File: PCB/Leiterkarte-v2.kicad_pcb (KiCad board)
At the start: 4 copper layers, 82 parts, among them J1 MSD-1-A, SW33V1 Conn_01x01_Pin

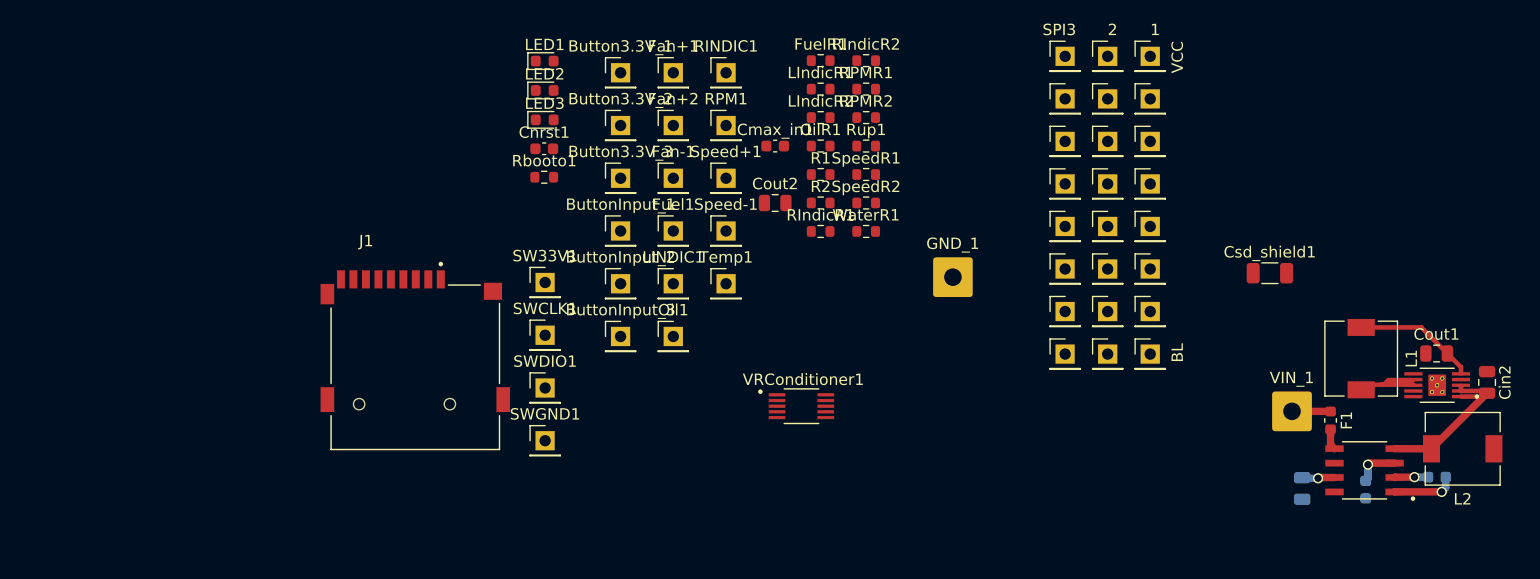
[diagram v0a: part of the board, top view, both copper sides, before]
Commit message: Updated component selection; Updated some footprints; Added .csv file in the export folder of the PCB that contains parts from DigiKey
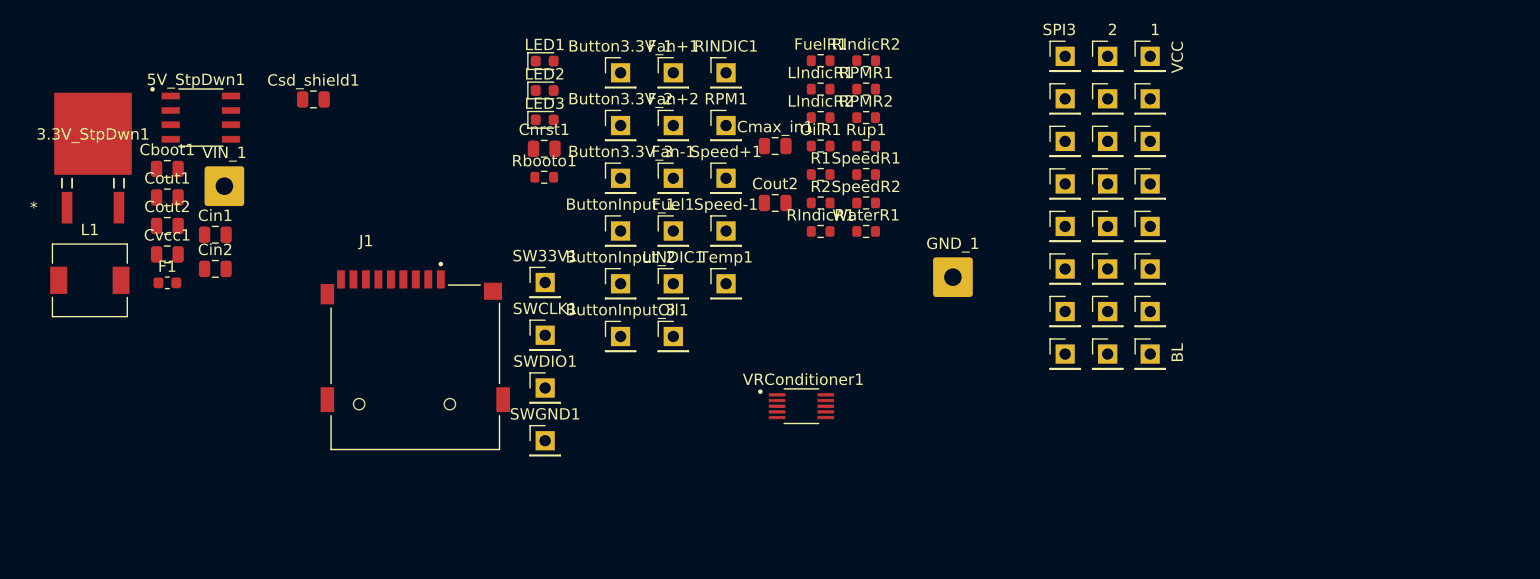
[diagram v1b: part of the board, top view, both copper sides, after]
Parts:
- removed L2: 33uH, Inductor_SMD:L_6.3x6.3_H3
- added Cout2: 10uF, Capacitor_SMD:C_0805_2012Metric, F.Cu at (99.8, 43.5)
- 3.3V_StpDwn1: value TPS62046DGQR -> NCV33269DTRK3.3G; footprint TPS62046DGQR:IC_XTR111AIDGQR -> NCV33269DTRK3.3G:DPAK-3_ONS-M
- Cboot1, Cvcc1: footprint Capacitor_SMD:C_0603_1608Metric -> Capacitor_SMD:C_0805_2012Metric; moved to F.Cu
- Cin1: moved to F.Cu
- Cmax_in1, Cnrst1: footprint Capacitor_SMD:C_0603_1608Metric -> Capacitor_SMD:C_0805_2012Metric
- Csd_shield1: footprint Capacitor_SMD:C_1206_3216Metric -> Capacitor_SMD:C_0805_2012Metric
- L1: value 6.2uH -> 33uH
- moved 3.3V_StpDwn1 120.6 mm to (93.3, 35.4), turned to 0 degrees
- moved Cboot1 115.2 mm to (99.8, 38.4), turned to 0 degrees
- moved Cout1 112.7 mm to (99.8, 40.9)
- moved Cin2 112.6 mm to (104.1, 47.2), turned to 0 degrees
- moved L1 112.3 mm to (93.0, 48.2), turned to 0 degrees
- moved Cvcc1 107.7 mm to (99.8, 46.0), turned to 0 degrees
- moved 5V_StpDwn1 107.2 mm to (102.8, 33.9), turned to 0 degrees
- moved F1 103.3 mm to (99.8, 48.5), turned to 0 degrees
- moved Cin1 98.4 mm to (104.1, 44.2), turned to 0 degrees
- moved VIN_1 96.2 mm to (104.9, 40.0)
- moved Csd_shield1 85.7 mm to (112.7, 32.3)
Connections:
- 3.3V_StpDwn1 pad 1: 5V -> GND
- 3.3V_StpDwn1 pad 2: 5V -> 3.3V
- Cout1 pad 1: GND -> 5V
- Cout1 pad 2: 3.3V -> GND
- L1 pad 1: 3.3V -> Net-(5V_StpDwn1-SW)
- L1 pad 2: Net-(3.3V_StpDwn1-SW) -> 5V
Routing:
- net 5V: track 15.4 -> 0.00 mm
- net 3.3V: track 10.8 -> 0.00 mm
- net Net-(3.3V_StpDwn1-SW): track 7.75 -> 0.00 mm
- net Net-(5V_StpDwn1-SW): track 6.02 -> 0.00 mm, vias 1 -> 0
- net Net-(5V_StpDwn1-EN/CLKIN): track 4.74 -> 0.00 mm, vias 1 -> 0
- net Net-(5V_StpDwn1-VCC): track 3.92 -> 0.00 mm, vias 1 -> 0
- net Net-(VIN_1-Pin_1): track 3.41 -> 0.00 mm
- net Net-(5V_StpDwn1-BOOT): track 2.96 -> 0.00 mm, vias 1 -> 0

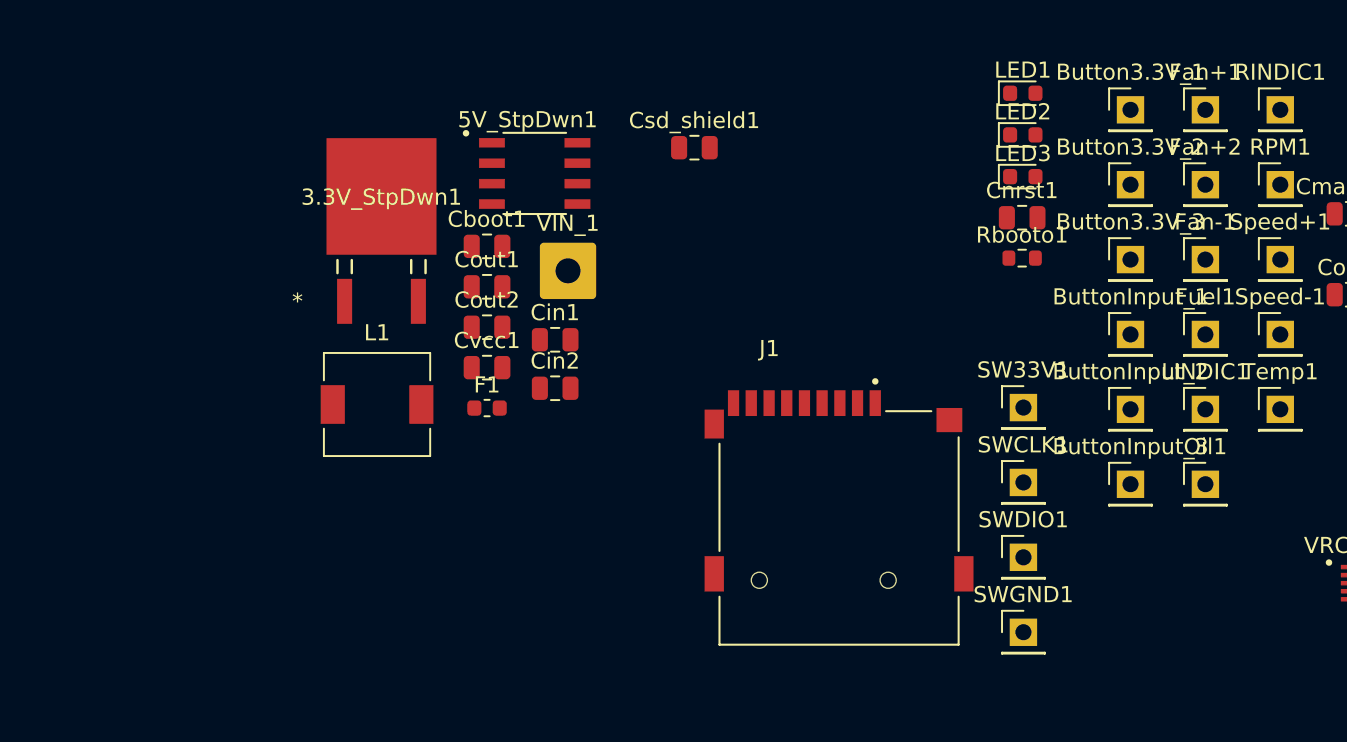
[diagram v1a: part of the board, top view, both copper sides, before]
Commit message: Replaced some global labels with power net(s); Added warning label for missing component
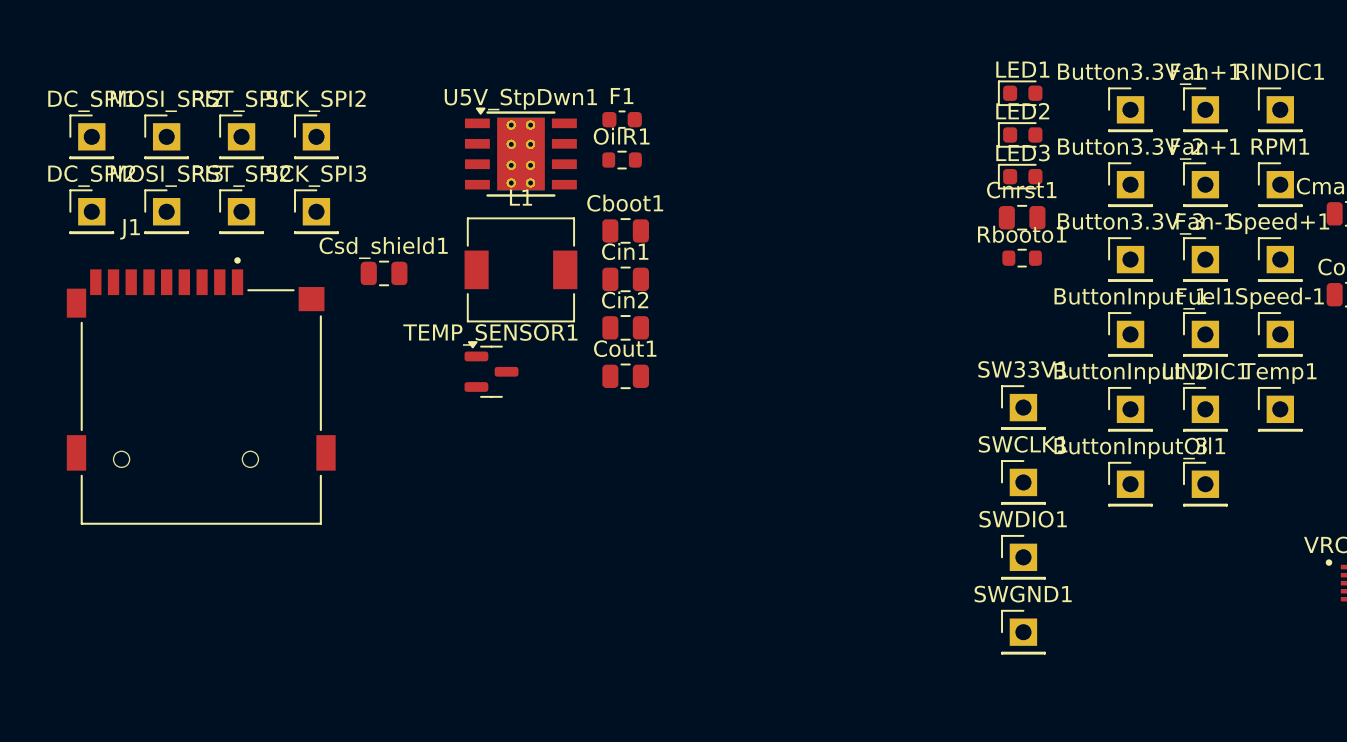
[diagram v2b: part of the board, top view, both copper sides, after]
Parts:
- removed 3.3V_StpDwn1: NCV33269DTRK3.3G, NCV33269DTRK3.3G:DPAK-3_ONS-M
- removed 5V_StpDwn1: L6981N50DR, L6981N50DR:SOIC127P600X175-8N
- removed the Cout2 at (99.8, 43.5)
- removed Cvcc1: 1uF, Capacitor_SMD:C_0805_2012Metric
- removed VIN_1: Conn_01x01_Pin, Connector_Wire:SolderWire-0.75sqmm_1x01_D1.25mm_OD3.5mm
- added DC_SPI1: Conn_01x01_Pin, Connector_PinHeader_2.54mm:PinHeader_1x01_P2.54mm_Vertical, F.Cu at (75.3, 31.6)
- added DC_SPI2: Conn_01x01_Pin, Connector_PinHeader_2.54mm:PinHeader_1x01_P2.54mm_Vertical, F.Cu at (75.3, 36.3)
- added MOSI_SPI2: Conn_01x01_Pin, Connector_PinHeader_2.54mm:PinHeader_1x01_P2.54mm_Vertical, F.Cu at (80.0, 31.6)
- added MOSI_SPI3: Conn_01x01_Pin, Connector_PinHeader_2.54mm:PinHeader_1x01_P2.54mm_Vertical, F.Cu at (80.0, 36.3)
- added OilR1: 100, Resistor_SMD:R_0603_1608Metric, F.Cu at (108.2, 33.1)
- added RST_SPI1: Conn_01x01_Pin, Connector_PinHeader_2.54mm:PinHeader_1x01_P2.54mm_Vertical, F.Cu at (84.6, 31.6)
- added RST_SPI2: Conn_01x01_Pin, Connector_PinHeader_2.54mm:PinHeader_1x01_P2.54mm_Vertical, F.Cu at (84.6, 36.3)
- added SCK_SPI2: Conn_01x01_Pin, Connector_PinHeader_2.54mm:PinHeader_1x01_P2.54mm_Vertical, F.Cu at (89.2, 31.6)
- added SCK_SPI3: Conn_01x01_Pin, Connector_PinHeader_2.54mm:PinHeader_1x01_P2.54mm_Vertical, F.Cu at (89.2, 36.3)
- added TEMP_SENSOR1: MCP9700Ax-ETT, Package_TO_SOT_SMD:SOT-23, F.Cu at (100.1, 46.2)
- added U5V_StpDwn1: TPS5430DDA, Package_SO:TI_SO-PowerPAD-8_ThermalVias, F.Cu at (102.0, 32.7)
- Cboot1: value 100nF -> 10nF
- Cin1: value 10uF -> 22uF
- Cout1: value 22uF -> 10uF
- L1: value 33uH -> 15uH
- moved J1 40.3 mm to (82.1, 48.4)
- moved Csd_shield1 20.8 mm to (93.5, 40.1)
- moved F1 19.8 mm to (108.2, 30.6)
- moved L1 12.2 mm to (102.0, 39.9)
- moved Cout1 10.2 mm to (108.5, 46.5)
- moved Cboot1 8.66 mm to (108.5, 37.5)
- moved Cin1 5.76 mm to (108.5, 40.5)
- moved Cin2 5.76 mm to (108.5, 43.5)
- renumbered Fan+2 to Fan+1
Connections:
- net Net-(5V_StpDwn1-EN/CLKIN) renamed VCC
- Button3.3V_1 pad 1: 3.3V -> +3.3V
- Button3.3V_2 pad 1: 3.3V -> +3.3V
- Button3.3V_3 pad 1: 3.3V -> +3.3V
- Cin2 pad 1: 5V -> +5V
- Cout1 pad 1: 5V -> GND
- Cout1 pad 2: GND -> +3.3V
- Fan+1 pad 1: 5V -> +5V
- FuelR1 pad 1: 3.3V -> +3.3V
- J1 pad 4: 3.3V -> +3.3V
- L1 pad 2: 5V -> +5V
- LED1 pad 1: GND -> Net-(LED1-K)
- LED2 pad 1: GND -> Net-(LED2-K)
- LED3 pad 1: GND -> Net-(LED3-K)
- Rbooto1 pad 1: GND -> +3.3V
- Rup1 pad 2: 5V -> +5V
- STM1 pad 100: 3.3V -> +3.3V
- STM1 pad 11: 3.3V -> +3.3V
- STM1 pad 16: Net-(MOSI_SPI3-Pin_1) -> TEMP1
- STM1 pad 18: unconnected-(STM1-PC3_C-Pad18) -> Net-(MOSI_SPI3-Pin_1)
- STM1 pad 20: 3.3V -> +3.3V
- STM1 pad 21: 3.3V -> +3.3V
- STM1 pad 24: unconnected-(STM1-PA2-Pad24) -> TEMP2
- STM1 pad 27: 3.3V -> +3.3V
- STM1 pad 50: 3.3V -> +3.3V
- STM1 pad 75: 3.3V -> +3.3V
- SW33V1 pad 1: 3.3V -> +3.3V
- VCC_SPI_1 pad 1: 5V -> +5V
- VCC_SPI_2 pad 1: 5V -> +5V
- VCC_SPI_3 pad 1: 5V -> +5V
- VRConditioner1 pad 10: 5V -> +5V
- WaterR1 pad 1: 3.3V -> +3.3V
